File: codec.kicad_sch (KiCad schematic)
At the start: 26 parts, among them U1 UDA1380HN_N2

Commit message: Added I2C pins
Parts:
- added R5: 10k, symbol Device:R
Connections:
- net V_3V0: now also R5.2
- net A1: now reaches U1.12 (L3MODE)
- net SCL: now reaches U1.13 (L3CLOCK/SCL)
- net SDA: now reaches U1.14 (L3DATA/SDA)
- net SEL_L3_IIC: now reaches U1.15 (SEL_L3_IIC)
- net SEL_L3_IIC: now also R5.1
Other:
- note added: "We set the pin to HIGH to use I2C mode (page 18)"
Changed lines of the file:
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@@
 	)
 	(junction
-		(at 85.09 130.81)
+		(at 86.36 134.62)
 		(diameter 0)
 		(color 0 0 0 0)
@@
 	(wire
 		(pts
-			(xy 85.09 128.27) (xy 85.09 130.81)
+			(xy 86.36 132.08) (xy 86.36 134.62)
 		)
 		(stroke
@@
 	(wire
 		(pts
-			(xy 85.09 130.81) (xy 88.9 130.81)
+			(xy 86.36 134.62) (xy 90.17 134.62)
 		)
 		(stroke
@@
 	(wire
 		(pts
+			(xy 191.77 54.61) (xy 186.69 54.61)
+		)
+		(stroke
+			(width 0)
+			(type default)
+		)
+	)
+	(wire
+		(pts
 			(xy 30.48 161.29) (xy 34.29 161.29)
 		)
@@
 		)
 	)
+	(wire
+		(pts
+			(xy 139.7 69.85) (xy 151.13 69.85)
+		)
+		(stroke
+			(width 0)
+			(type default)
+		)
+	)
 	(polyline
 		(pts
@@
 	(wire
 		(pts
-			(xy 81.28 130.81) (xy 85.09 130.81)
+			(xy 82.55 134.62) (xy 86.36 134.62)
 		)
 		(stroke
@@
 	(wire
 		(pts
+			(xy 144.78 92.71) (xy 151.13 92.71)
+		)
+		(stroke
+			(width 0)
+			(type default)
+		)
+	)
+	(wire
+		(pts
 			(xy 83.82 187.96) (xy 85.09 187.96)
 		)
@@
 	(text "Since we do not use microphone,\nthese can be connected to ground"
 		(exclude_from_sim no)
-		(at 85.09 123.952 0)
+		(at 86.36 127.762 0)
+		(effects
+			(font
+				(size 1.27 1.27)
+			)
+		)
+	)
+	(text "We set the pin to HIGH\nto use I2C mode (page 18)"
+		(exclude_from_sim no)
+		(at 54.864 39.624 0)
 		(effects
 			(font
@@
 		)
 	)
+	(label "SEL_L3_IIC"
+		(at 151.13 72.39 180)
+		(fields_autoplaced yes)
+		(effects
+			(font
+				(size 1.27 1.27)
+			)
+			(justify right bottom)
+		)
+	)
 	(label "VADCP"
 		(at 53.34 143.51 0)
@@
 	)
 	(label "VINR"
-		(at 88.9 130.81 0)
+		(at 90.17 134.62 0)
 		(fields_autoplaced yes)
 		(effects
@@
 	)
 	(label "VINL"
-		(at 81.28 130.81 180)
+		(at 82.55 134.62 180)
 		(fields_autoplaced yes)
 		(effects
@@
 	)
 	(label "VINM"
-		(at 85.09 128.27 0)
+		(at 86.36 132.08 0)
 		(fields_autoplaced yes)
 		(effects
@@
 		)
 	)
+	(label "SEL_L3_IIC"
+		(at 58.42 35.56 0)
+		(fields_autoplaced yes)
+		(effects
+			(font
+				(size 1.27 1.27)
+			)
+			(justify left bottom)
+		)
+	)
 	(label "VDDA(AD)"
 		(at 151.13 62.23 180)
@@
 		)
 	)
+	(hierarchical_label "SCL"
+		(shape input)
+		(at 139.7 69.85 180)
+		(fields_autoplaced yes)
+		(effects
+			(font
+				(size 1.27 1.27)
+			)
+			(justify right)
+		)
+	)
 	(hierarchical_label "SYSCLK"
 		(shape input)
@@
 		)
 	)
+	(hierarchical_label "SDA"
+		(shape bidirectional)
+		(at 191.77 54.61 0)
+		(fields_autoplaced yes)
+		(effects
+			(font
+				(size 1.27 1.27)
+			)
+			(justify left)
+		)
+	)
+	(hierarchical_label "A1"
+		(shape input)
+		(at 144.78 92.71 180)
+		(fields_autoplaced yes)
+		(effects
+			(font
+				(size 1.27 1.27)
+			)
+			(justify right)
+		)
+	)
 	(hierarchical_label "V_3V0"
 		(shape input)
@@
 		)
 	)
+	(hierarchical_label "V_3V0"
+		(shape input)
+		(at 50.8 35.56 180)
+		(fields_autoplaced yes)
+		(effects
+			(font
+				(size 1.27 1.27)
+			)
+			(justify right)
+		)
+	)
 	(symbol
 		(lib_id "power:GND")
@@
 	)
 	(symbol
+		(lib_id "Device:R")
+		(at 54.61 35.56 270)
+		(unit 1)
+		(exclude_from_sim no)
+		(in_bom yes)
+		(on_board yes)
+		(dnp no)
+		(property "Reference" "R5"
+			(at 54.61 30.988 90)
+			(effects
+				(font
+					(size 1.27 1.27)
+				)
+			)
+		)
+		(property "Value" "10k"
+			(at 54.61 33.528 90)
+			(effects
+				(font
+					(size 1.27 1.27)
+				)
+			)
+		)
+		(property "Footprint" ""
+			(at 54.61 33.782 90)
+			(effects
+				(font
+					(size 1.27 1.27)
+				)
+				(hide yes)
+			)
+		)
+		(property "Datasheet" "~"
+			(at 54.61 35.56 0)
+			(effects
+				(font
+					(size 1.27 1.27)
+				)
+				(hide yes)
+			)
+		)
+		(property "Description" "Resistor"
+			(at 54.61 35.56 0)
+			(effects
+				(font
+					(size 1.27 1.27)
+				)
+				(hide yes)
+			)
+		)
+		(pin "2"
+		)
+		(pin "1"
+		)
+		(instances
+			(project "plant caretaker"
+				(path "/23b35dcc-615e-4aec-abee-c26cc3d8b906/34ae70cd-ec6d-4009-8d65-9818ae1eafe0"
+					(reference "R5")
+					(unit 1)
+				)
+			)
+		)
+	)
+	(symbol
 		(lib_id "power:PWR_FLAG")
 		(at 101.6 157.48 0)
@@
 	(symbol
 		(lib_id "power:GND")
-		(at 85.09 130.81 0)
+		(at 86.36 134.62 0)
 		(mirror y)
 		(unit 1)
@@
 		(fields_autoplaced yes)
 		(property "Reference" "#PWR025"
-			(at 85.09 137.16 0)
+			(at 86.36 140.97 0)
 			(effects
 				(font
@@
 		)
 		(property "Value" "GND"
-			(at 85.09 135.89 0)
+			(at 86.36 139.7 0)
 			(effects
 				(font
@@
 		)
 		(property "Footprint" ""
-			(at 85.09 130.81 0)
+			(at 86.36 134.62 0)
 			(effects
 				(font
@@
 		)
 		(property "Datasheet" ""
-			(at 85.09 130.81 0)
+			(at 86.36 134.62 0)
 			(effects
 				(font
@@
 		)
 		(property "Description" "Power symbol creates a global label with name \"GND\" , ground"
-			(at 85.09 130.81 0)
+			(at 86.36 134.62 0)
 			(effects
 				(font

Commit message: Finished AudioAmplifier + Added Values
Added Buck Coverter components values, finished audio amplifier
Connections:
- net OUT_L renamed Left Speaker Input
- net OUT_R renamed Right Speaker Input
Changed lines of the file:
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@@
 		)
 	)
-	(hierarchical_label "OUT_L"
+	(hierarchical_label "Left Speaker Input"
 		(shape output)
 		(at 252.73 68.58 0)
@@
 		)
 	)
-	(hierarchical_label "OUT_R"
+	(hierarchical_label "Right Speaker Input"
 		(shape output)
 		(at 252.73 63.5 0)

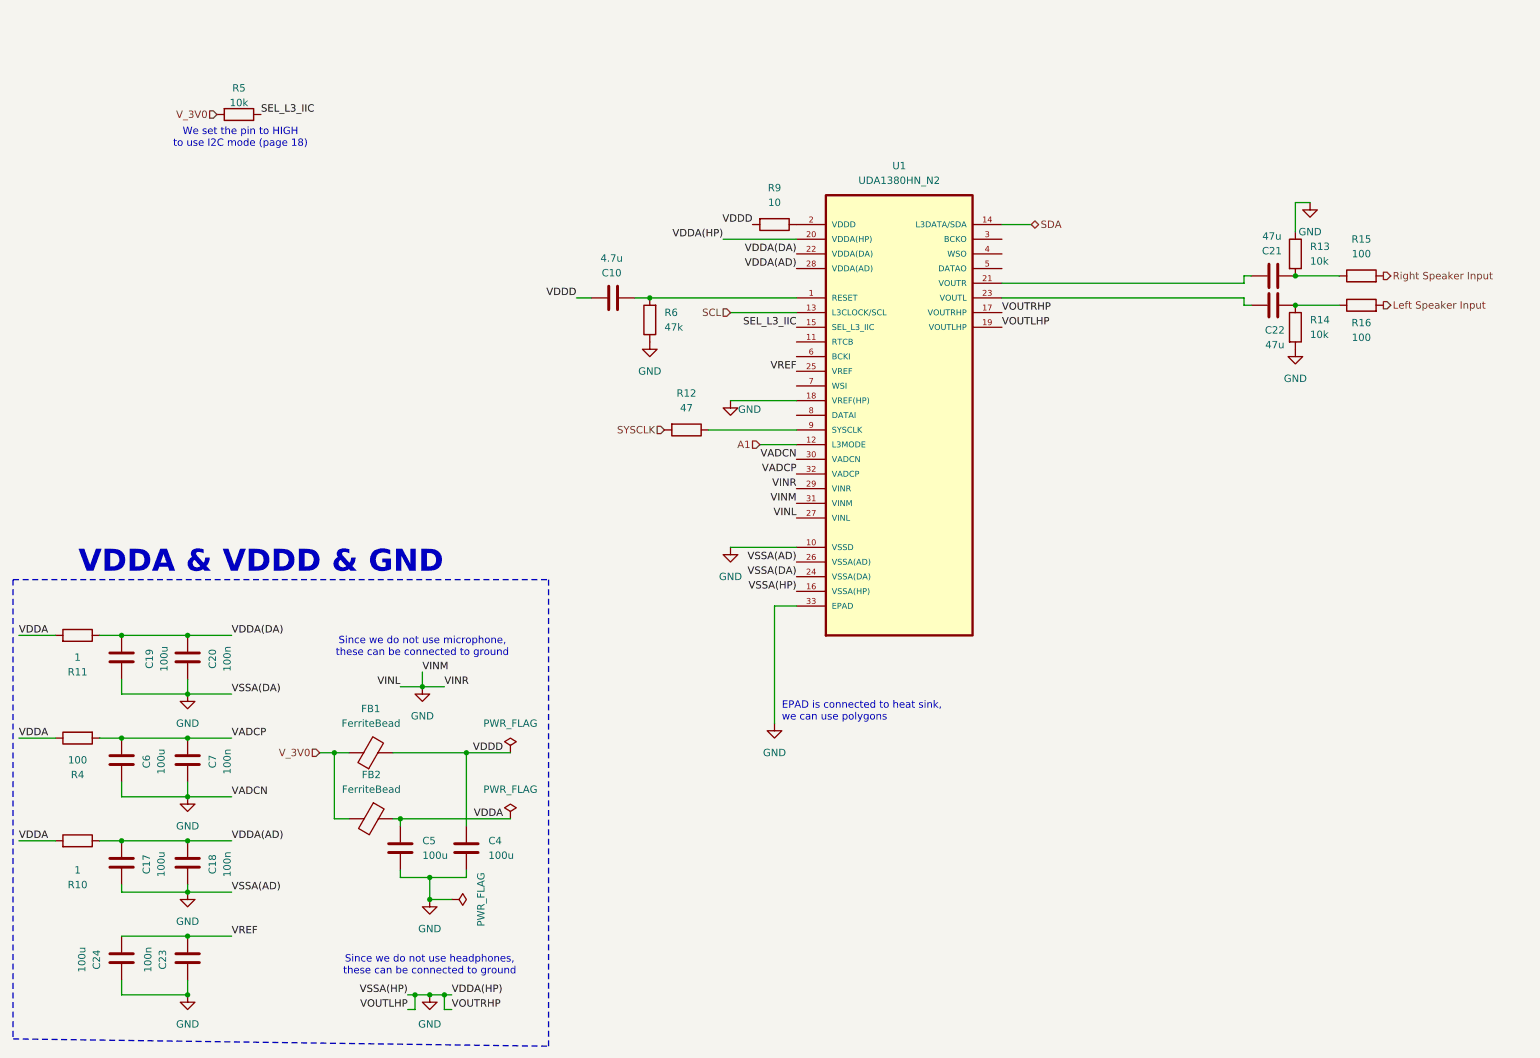
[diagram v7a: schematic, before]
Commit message: Fixed connections and digital output of codec
Used NC instead of GND for output pins
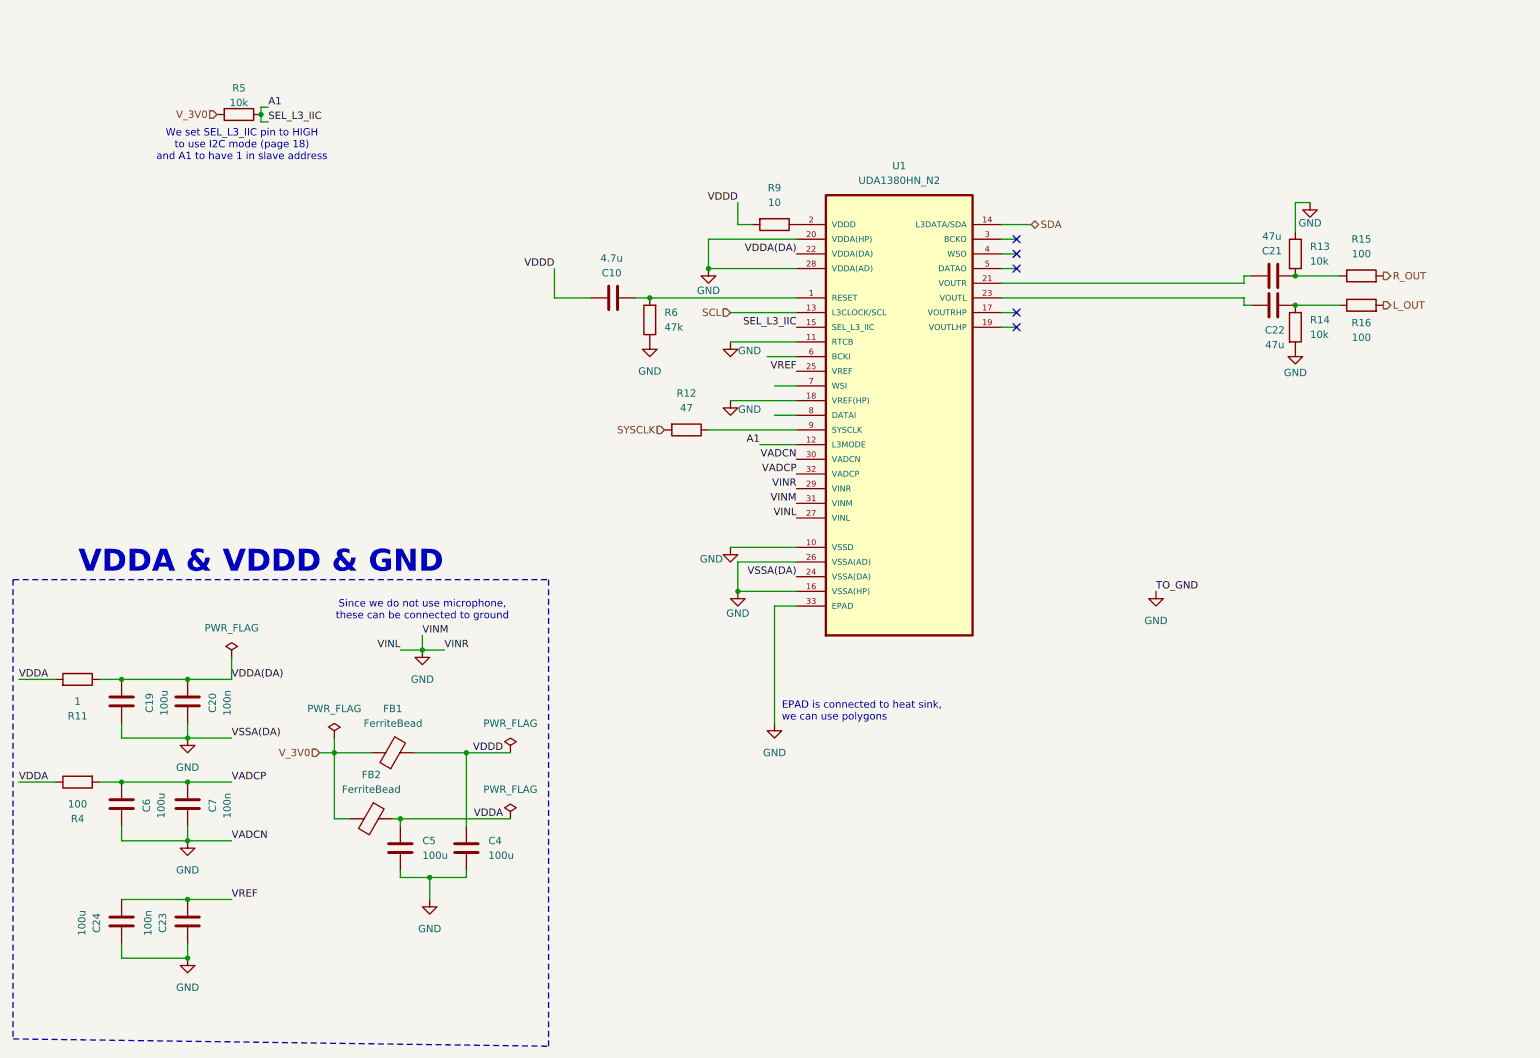
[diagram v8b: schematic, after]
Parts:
- removed C17: 100u, symbol Device:C
- removed C18: 100n, symbol Device:C
- removed R10: 1, symbol Device:R
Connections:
- net SEL_L3_IIC is gone; now on net A1: R5.1, U1.15 (SEL_L3_IIC)
- net VDDA(AD) is gone; now on net GND: U1.28 (VDDA(AD))
- net GND: now also U1.11 (RTCB); no longer U1.17 (VOUTRHP), U1.19 (VOUTLHP)
- net Left Speaker Input renamed L_OUT
- net Right Speaker Input renamed R_OUT
- no-connect marks 0 -> 5
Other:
- note added: "We set SEL_L3_IIC pin to HIGH to use I2C mode (page 18) and A1 to have 1 in slave address"
- note removed: "Since we do not use headphones, these can be connected to ground"
- note removed: "We set the pin to HIGH to use I2C mode (page 18)"
- moved on the sheet: C19, C20, C23, C24, C6, C7, FB1, R11, R4
